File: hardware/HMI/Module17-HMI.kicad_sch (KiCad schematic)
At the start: 59 parts, among them J1 Hirose FH12-26S-0.5SH(55), J3 Hirose FH12A-24S-0.5SH(55), Q1 MMBT3904, Q2 BSS84, SW9 CL-SB-22A-1x, U1 TPS61040DBV, U2 AP7375-33SA, U3 IQS211B00000000TS, U4 CAP1206-x-SL

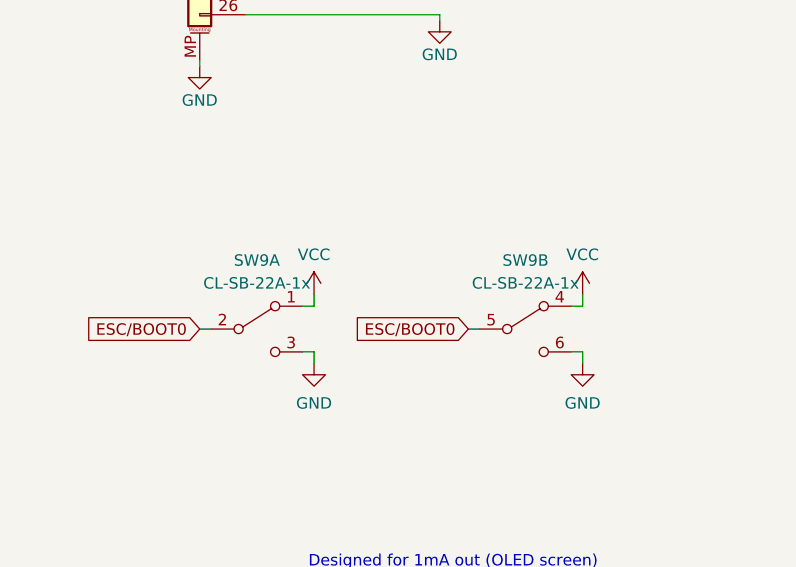
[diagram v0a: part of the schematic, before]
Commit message: Updated HMI boards
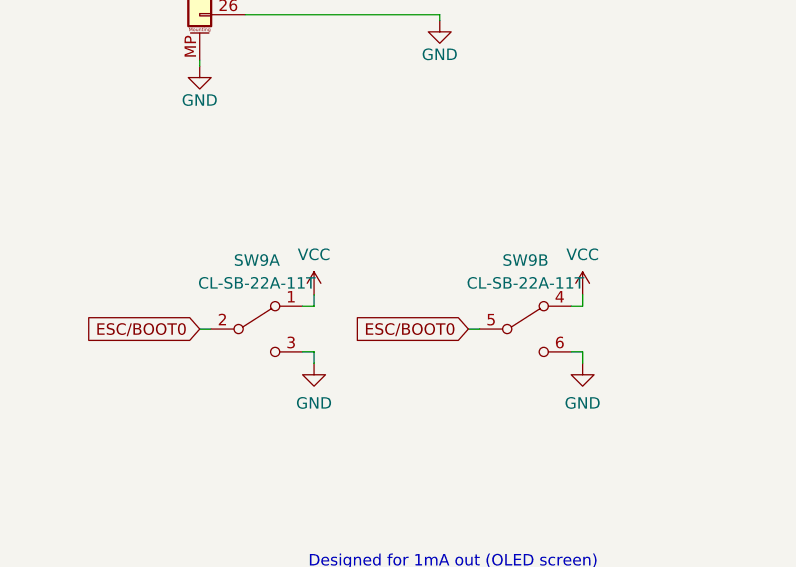
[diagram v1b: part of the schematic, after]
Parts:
- C1, C16: MPN (none) -> Generic C 4u7/X7R/25V/0805
- C10, C11, C13, C15, C3, C4, C5: MPN (none) -> Generic C 1u/X7R/25V/0603
- C12: MPN (none) -> Generic C 10p/C0G/16V/0603
- C14: MPN (none) -> Generic C 2u2/X7R/25V/0805
- C17, C8: MPN (none) -> Generic C 100n/X7R/25V/0603
- C2: MPN (none) -> Generic C 15p/C0G/16V/0603
- C6, C9: MPN (none) -> Generic C 100p/C0G/16V/0603
- C7: MPN (none) -> Generic C 10u/X7R/16V/0805
- D1: MPN (none) -> Generic Schottky Diode
- D3: MPN LTST-C230KAKT, LTST-C230KGKT, LTST-C230KRKT, LTST-C230KSKT -> LTST-C230KRKT
- J1: LCSC Part # (none) -> C202113; MPN (none) -> Hirose FH12-26S-0.5SH(55)
- J3: LCSC Part # (none) -> C506794; MPN (none) -> Hirose FH12A-24S-0.5SH(55)
- L1: MPN (none) -> Generic L/1u/1008
- Q1: MPN (none) -> MMBT3904
- Q2: MPN (none) -> BSS84
- R1: MPN (none) -> Generic R/1M37/0603
- R10, R11, R12, R16, R9: MPN (none) -> Generic R/680/0603
- R13, R14, R15, R17: MPN (none) -> Generic R/10k/0603
- R2: MPN (none) -> Generic R/150k/0603
- R3, R5, R6: MPN (none) -> Generic R/1k2/0603
- R4: MPN (none) -> Generic R/40/0603
- R7: MPN (none) -> Generic R/470/0603
- R8: MPN (none) -> Generic R/910k/0603
- SW9: value CL-SB-22A-1x -> CL-SB-22A-11T; footprint M17_misc_passive:Nidec_Copal-SB-22A -> M17_misc_passive:Nidec_Copal-SB-22A_edge; MPN (none) -> CL-SB-22A-11T
- U1: LCSC Part # (none) -> C7722; MPN (none) -> TPS61040DBV
- U2: LCSC Part # (none) -> C5944186; MPN (none) -> AP7375-33SA
- U3: MPN (none) -> IQS211B00000000TS
- U4: MPN (none) -> CAP1206-1-SL

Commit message: Updated HMI
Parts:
- R4: value 40R -> 40.2; MPN Generic R/40/0603 -> Generic R/40.2/0603
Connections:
- net GND: now also J3.13 (Pin_13), J3.14 (Pin_14), J3.21 (Pin_21), J3.22 (Pin_22), J3.23 (Pin_23), J3.5 (Pin_5), J3.8 (Pin_8), J3.9 (Pin_9); no longer J3.11 (Pin_11), J3.12 (Pin_12), J3.16 (Pin_16), J3.17 (Pin_17), J3.2 (Pin_2), J3.20 (Pin_20), J3.3 (Pin_3), J3.4 (Pin_4)
- net OLED_CS: now also J3.17 (Pin_17); no longer J3.8 (Pin_8)
- net OLED_DC: now also J3.15 (Pin_15); no longer J3.10 (Pin_10)
- net OLED_RST: now also J3.16 (Pin_16); no longer J3.9 (Pin_9)
- net OLED_SPI_MOSI: now also J3.11 (Pin_11); no longer J3.14 (Pin_14)
- net OLED_SPI_SCK: now also J3.12 (Pin_12); no longer J3.13 (Pin_13)
- net VCC: now also J3.2 (Pin_2); no longer J3.23 (Pin_23)
- net VDD: now also J3.20 (Pin_20); no longer J3.5 (Pin_5)
- net at R8.1: now also J3.4 (Pin_4); no longer J3.21 (Pin_21)
- net at C14.1: now also J3.3 (Pin_3); no longer J3.22 (Pin_22)
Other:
- note removed: "16V"
- note removed: "25V"

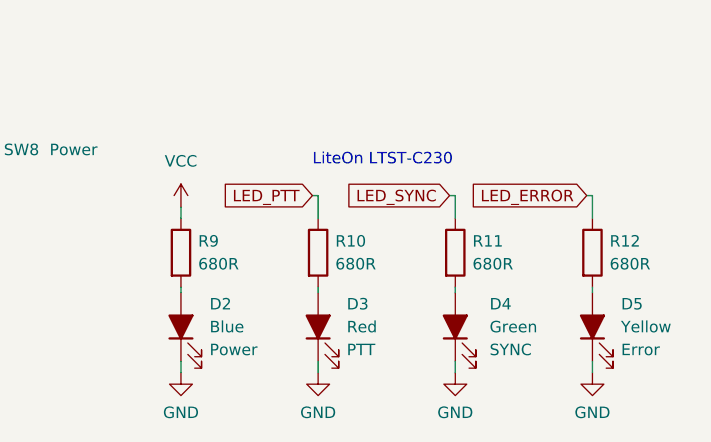
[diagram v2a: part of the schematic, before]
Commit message: Updated HMI
Added JLCPCB placeholder for batch number, removed useless texts
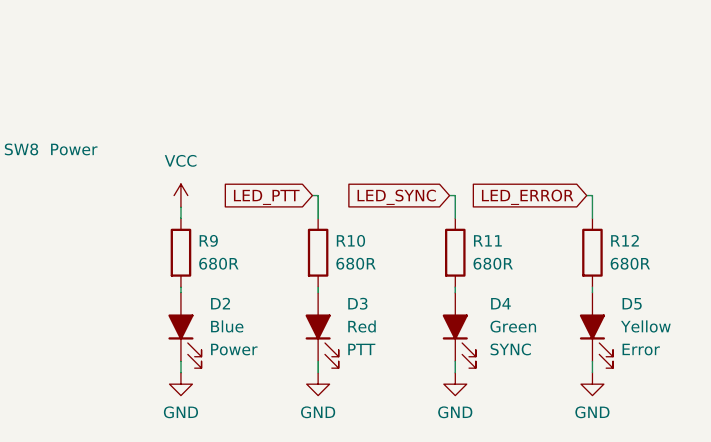
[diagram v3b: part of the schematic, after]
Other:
- note removed: "LiteOn LTST-C230"
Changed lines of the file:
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@@
-    (effects (font (size 1.27 1.27)) (justify left bottom))
-  )
-  (text "LiteOn LTST-C230" (at 240.665 33.02 0)
     (effects (font (size 1.27 1.27)) (justify left bottom))
   )

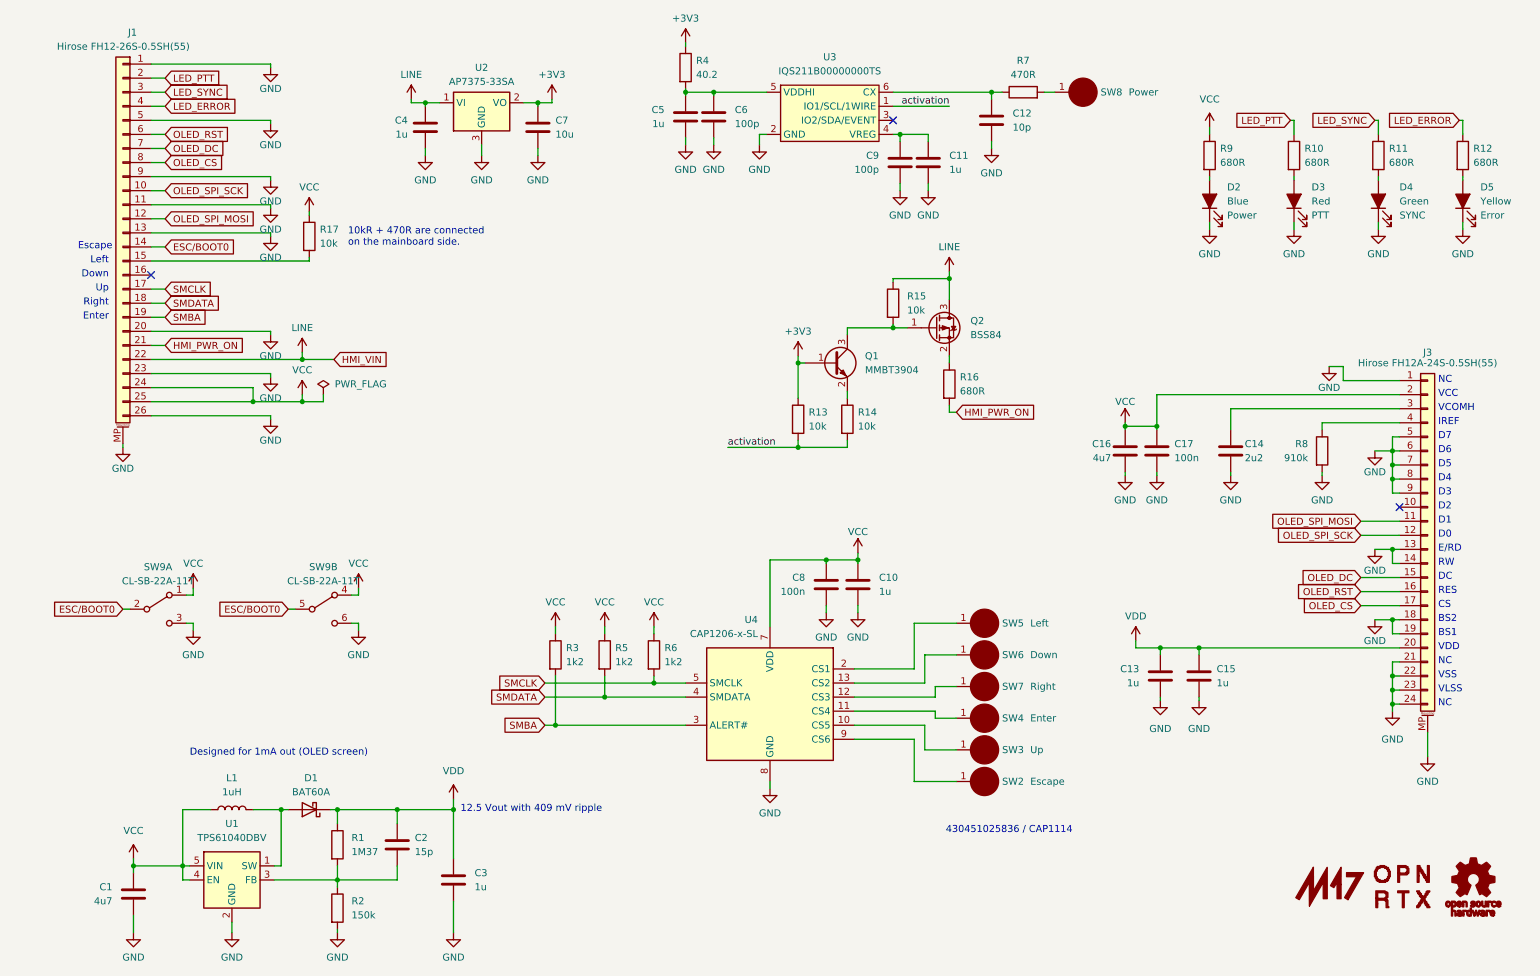
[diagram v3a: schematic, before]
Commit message: Updated HMI board
Fixed OLED screen power supply (VCC/VDD swapped).
Fixed Mainboard connector pinout.
Widened board.
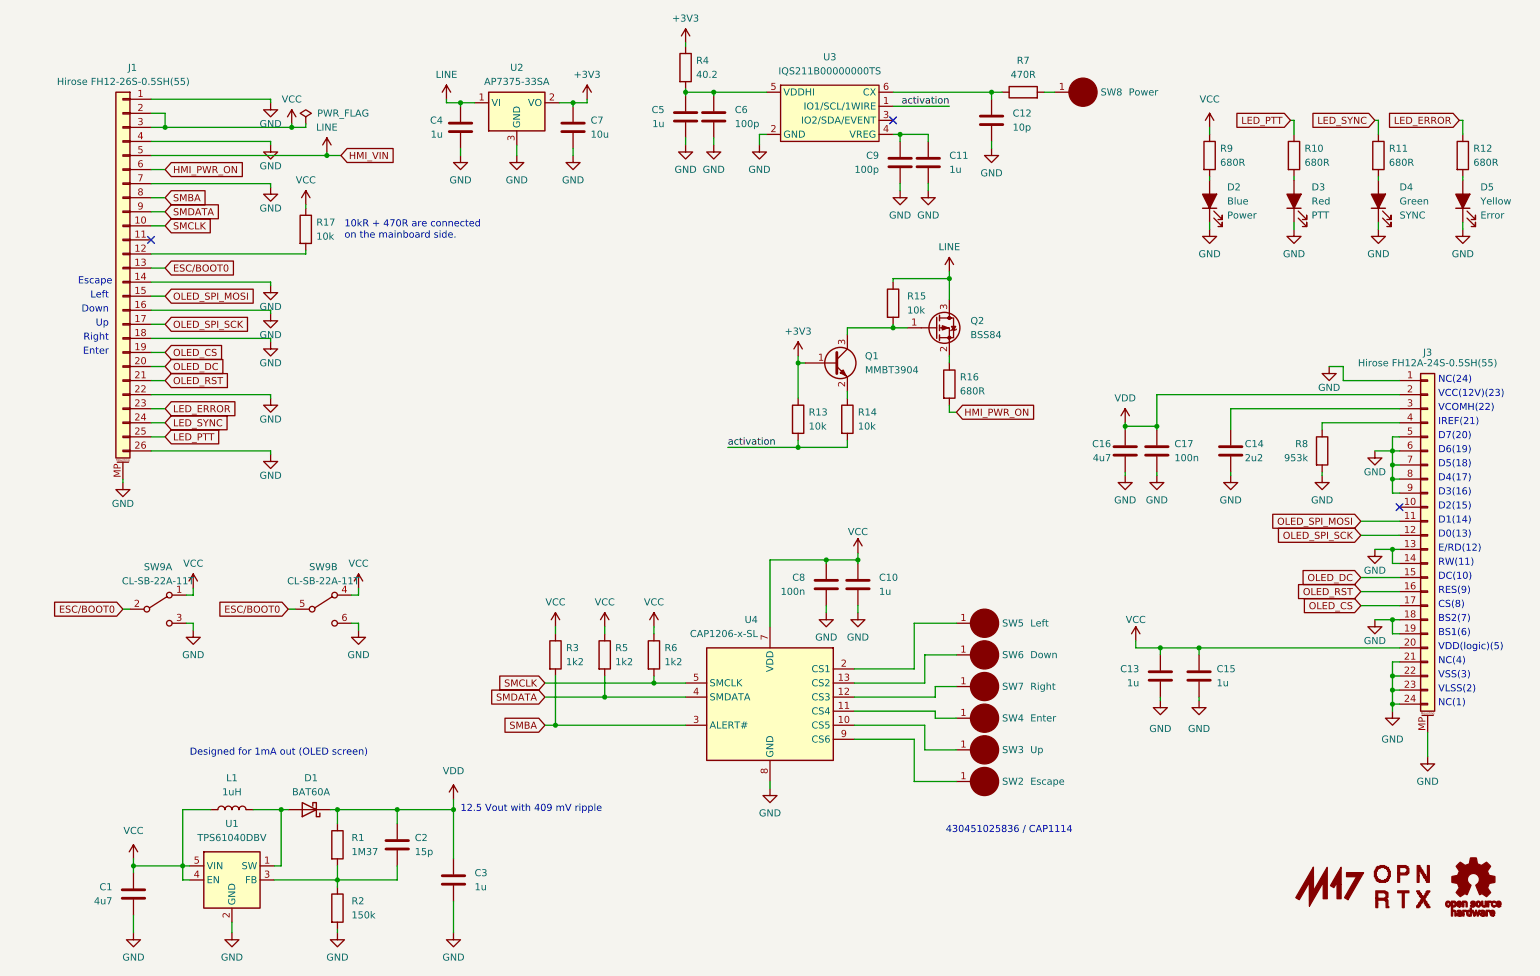
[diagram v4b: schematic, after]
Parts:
- R8: value 910k -> 953k; MPN Generic R/910k/0603 -> Generic R/953k/0603
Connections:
- net ESC/BOOT0: now also J1.13 (Pin_13); no longer J1.14 (Pin_14)
- net GND: now also J1.14 (Pin_14), J1.16 (Pin_16), J1.18 (Pin_18), J1.22 (Pin_22), J1.4 (Pin_4), J1.7 (Pin_7); no longer J1.11 (Pin_11), J1.13 (Pin_13), J1.20 (Pin_20), J1.23 (Pin_23), J1.5 (Pin_5), J1.9 (Pin_9)
- net HMI_PWR_ON: now also J1.6 (Pin_6); no longer J1.21 (Pin_21)
- net LED_ERROR: now also J1.23 (Pin_23); no longer J1.4 (Pin_4)
- net LED_PTT: now also J1.25 (Pin_25); no longer J1.2 (Pin_2)
- net LED_SYNC: now also J1.24 (Pin_24); no longer J1.3 (Pin_3)
- net LINE: now also J1.5 (Pin_5); no longer J1.22 (Pin_22)
- net OLED_CS: now also J1.19 (Pin_19); no longer J1.8 (Pin_8)
- net OLED_DC: now also J1.20 (Pin_20); no longer J1.7 (Pin_7)
- net OLED_RST: now also J1.21 (Pin_21); no longer J1.6 (Pin_6)
- net OLED_SPI_MOSI: now also J1.15 (Pin_15); no longer J1.12 (Pin_12)
- net OLED_SPI_SCK: now also J1.17 (Pin_17); no longer J1.10 (Pin_10)
- net SMBA: now also J1.8 (Pin_8); no longer J1.19 (Pin_19)
- net SMCLK: now also J1.10 (Pin_10); no longer J1.17 (Pin_17)
- net SMDATA: now also J1.9 (Pin_9); no longer J1.18 (Pin_18)
- net VCC: now also C13.1, C15.1, J1.2 (Pin_2), J1.3 (Pin_3), J3.20 (Pin_20); no longer C16.1, C17.1, J1.24 (Pin_24), J1.25 (Pin_25), J3.2 (Pin_2)
- net VDD: now also C16.1, C17.1, J3.2 (Pin_2); no longer C13.1, C15.1, J3.20 (Pin_20)
- net at R17.2: now also J1.12 (Pin_12); no longer J1.15 (Pin_15)
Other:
- note added: "BS1(6)"
- note added: "BS2(7)"
- note added: "CS(8)"
- note added: "D0(13)"
- note added: "D1(14)"
- note added: "D2(15)"
- note added: "D3(16)"
- note added: "D4(17)"
- note added: "D5(18)"
- note added: "D6(19)"
- note added: "D7(20)"
- note added: "DC(10)"
- note added: "E/RD(12)"
- note added: "IREF(21)"
- note added: "NC(1)"
- note added: "NC(24)"
- note added: "NC(4)"
- note added: "RES(9)"
- note added: "RW(11)"
- note added: "VCC(12V)(23)"
- note added: "VCOMH(22)"
- note added: "VDD(logic)(5)"
- note added: "VLSS(2)"
- note added: "VSS(3)"
- note removed: "BS1"
- note removed: "BS2"
- note removed: "CS"
- note removed: "D0"
- note removed: "D1"
- note removed: "D2"
- note removed: "D3"
- note removed: "D4"
- note removed: "D5"
- note removed: "D6"
- note removed: "D7"
- note removed: "DC"
- note removed: "E/RD"
- note removed: "IREF"
- note removed: "NC"
- note removed: "RES"
- note removed: "RW"
- note removed: "VCC"
- note removed: "VCOMH"
- note removed: "VDD"
- note removed: "VLSS"
- note removed: "VSS"
- moved on the sheet: C4, C7, J1, U2

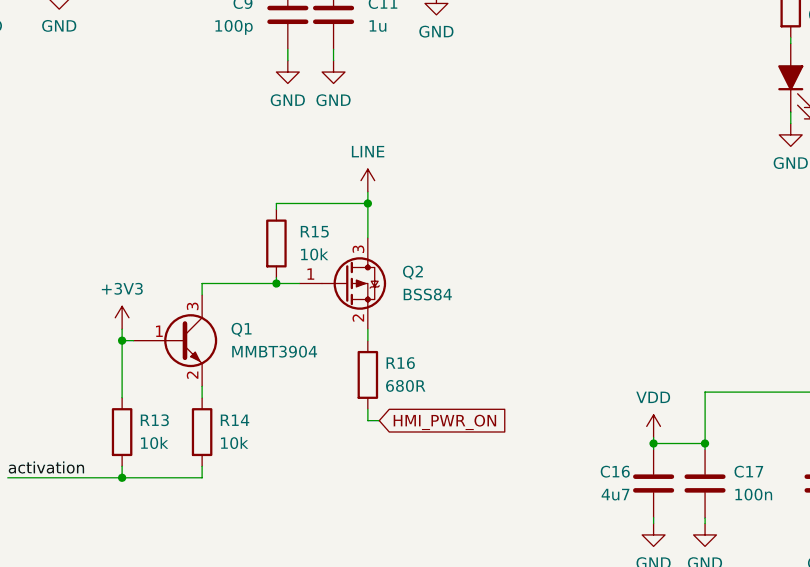
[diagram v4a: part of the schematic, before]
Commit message: Fixed power button Q2  connected in reverse
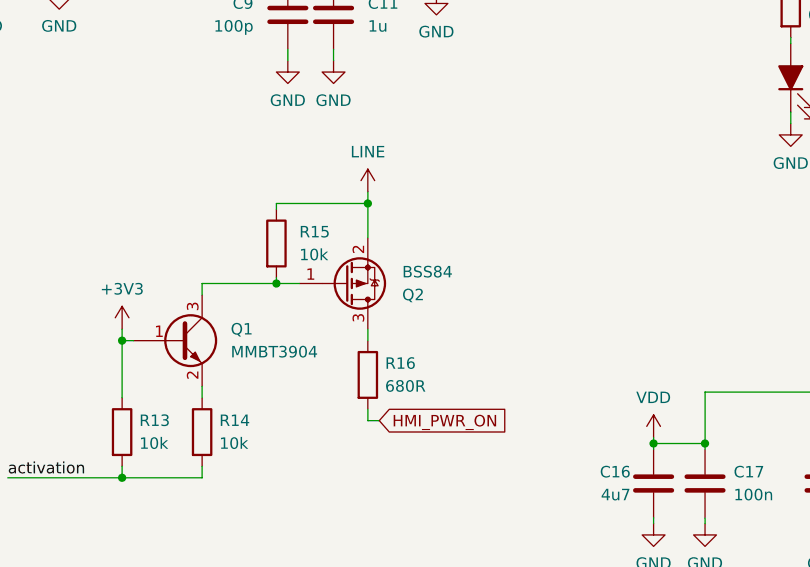
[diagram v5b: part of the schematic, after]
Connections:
- net LINE: now also Q2.2 (S); no longer Q2.3 (D)
- net at R16.1: now also Q2.3 (D); no longer Q2.2 (S)
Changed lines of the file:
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@@
     )
   )
-  (symbol (lib_id "Transistor_FET:BSS84") (at 176.53 73.66 0) (unit 1)
-    (in_bom yes) (on_board yes) (dnp no) (fields_autoplaced)
-    (property "Reference" "Q2" (at 182.88 72.39 0)
+  (symbol (lib_id "Transistor_FET:BSS84") (at 176.53 73.66 0) (mirror x) (unit 1)
+    (in_bom yes) (on_board yes) (dnp no)
+    (property "Reference" "Q2" (at 182.88 74.93 0)
       (effects (font (size 1.27 1.27)) (justify left))
     )
-    (property "Value" "BSS84" (at 182.88 74.93 0)
+    (property "Value" "BSS84" (at 182.88 72.39 0)
       (effects (font (size 1.27 1.27)) (justify left))
     )
-    (property "Footprint" "Package_TO_SOT_SMD:SOT-23" (at 181.61 75.565 0)
+    (property "Footprint" "Package_TO_SOT_SMD:SOT-23" (at 181.61 71.755 0)
       (effects (font (size 1.27 1.27) italic) (justify left) hide)
     )

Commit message: Updated HMI to Rev 0.99b
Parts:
- D2: LCSC Part # (none) -> C125109
- D3: LCSC Part # (none) -> C125107
- D4: LCSC Part # (none) -> C125106
- D5: LCSC Part # (none) -> C125108

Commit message: Updated HMI PCB to revision 1.0
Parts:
- U4: value CAP1206-x-SL -> CAP1206-1-SL
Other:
- company: (none) -> M17 Project
- title: (none) -> Module17 HMI
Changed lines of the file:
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@@
 	(generator_version "8.0")
 	(paper "A4")
+	(title_block
+		(title "Module17 HMI")
+		(date "2024-06-19")
+		(rev "Rev 1.0")
+		(company "M17 Project")
+		(comment 1 "Morgan - ON4MOD")
+		(comment 2 "Authors:")
+	)
 	(junction
 		(at 162.56 115.57)
@@
 			)
 		)
-		(property "Value" "CAP1206-x-SL"
+		(property "Value" "CAP1206-1-SL"
 			(at 144.4909 128.905 0)
 			(effects

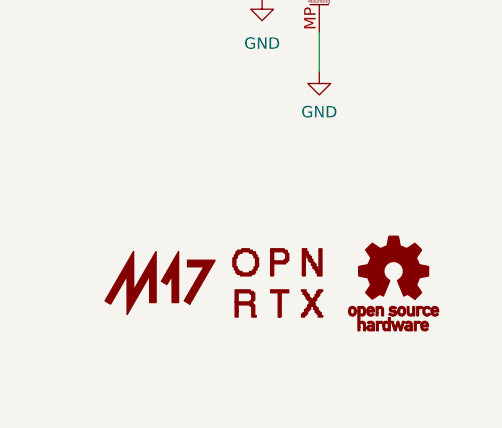
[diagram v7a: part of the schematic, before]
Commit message: Added OSHWA certification mark
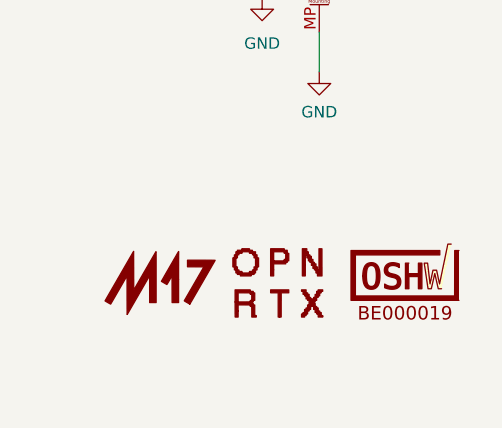
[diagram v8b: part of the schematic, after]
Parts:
- removed LOGO3: OSHW_logo, M17_logos:OSHW_logo_12.5x13mm, symbol M17_logos:OSHW_logo
- added LOGO101: ~, OSHW_Certification_Mark:OSHW-Certification-Mark-Stacked_12x10mm_SilkMask, symbol OSHW_Certification_Mark:OSHW_Certification_Mark_Stacked_Medium
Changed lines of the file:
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@@
+	)
+	(symbol
+		(lib_id "OSHW_Certification_Mark:OSHW_Certification_Mark_Stacked_Medium")
+		(at 274.955 173.355 0)
+		(unit 1)
+		(exclude_from_sim no)
+		(in_bom no)
+		(on_board yes)
+		(dnp no)
+		(fields_autoplaced yes)
+		(property "Reference" "LOGO101"
+			(at 274.955 173.355 0)
+			(effects
+				(font
+					(size 1.27 1.27)
+				)
+				(hide yes)
+			)
+		)
+		(property "Value" "~"
+			(at 274.955 173.355 0)
+			(effects
+				(font
+					(size 1.27 1.27)
+				)
+				(hide yes)
+			)
+		)
+		(property "Footprint" "OSHW_Certification_Mark:OSHW-Certification-Mark-Stacked_12x10mm_SilkMask"
+			(at 274.955 173.355 0)
+			(effects
+				(font
+					(size 1.27 1.27)
+				)
+				(hide yes)
+			)
+		)
+		(property "Datasheet" ""
+			(at 274.955 173.355 0)
+			(effects
+				(font
+					(size 1.27 1.27)
+				)
+				(hide yes)
+			)
+		)
+		(property "Description" "OSHW Certification Mark, Stacked"
+			(at 274.955 173.355 0)
+			(effects
+				(font
+					(size 1.27 1.27)
+				)
+				(hide yes)
+			)
+		)
+		(instances
+			(project ""
+				(path "/a2e72162-b48d-4c58-b01e-f32423724fdc"
+					(reference "LOGO101")
+					(unit 1)
+				)
+			)
+		)
 	)
 	(symbol
@@
 					(unit 1)
 				)
-			)
-		)
-	)
-	(symbol
-		(lib_id "M17_logos:OSHW_logo")
-		(at 273.685 174.625 0)
-		(unit 1)
-		(exclude_from_sim no)
-		(in_bom no)
-		(on_board yes)
-		(dnp no)
-		(fields_autoplaced yes)
-		(property "Reference" "LOGO3"
-			(at 273.685 170.0012 0)
-			(effects
-				(font
-					(size 1.27 1.27)
-				)
-				(hide yes)
-			)
-		)
-		(property "Value" "OSHW_logo"
-			(at 273.685 179.2488 0)
-			(effects
-				(font
-					(size 1.27 1.27)
-				)
-				(hide yes)
-			)
-		)
-		(property "Footprint" "M17_logos:OSHW_logo_12.5x13mm"
-			(at 273.685 174.625 0)
-			(effects
-				(font
-					(size 1.27 1.27)
-				)
-				(hide yes)
-			)
-		)
-		(property "Datasheet" ""
-			(at 273.685 174.625 0)
-			(effects
-				(font
-					(size 1.27 1.27)
-				)
-				(hide yes)
-			)
-		)
-		(property "Description" ""
-			(at 273.685 174.625 0)
-			(effects
-				(font
-					(size 1.27 1.27)
-				)
-				(hide yes)
-			)
-		)
-		(property "LCSC Part #" ""
-			(at 273.685 174.625 0)
-			(effects
-				(font
-					(size 1.27 1.27)
-				)
-				(hide yes)
-			)
-		)
-		(instances
-			(project "Module17-HMI"
-				(path "/a2e72162-b48d-4c58-b01e-f32423724fdc"
-					(reference "LOGO3")
-					(unit 1)
-				)
